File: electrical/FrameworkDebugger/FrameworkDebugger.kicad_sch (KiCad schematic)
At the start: 7 parts, among them J4 Conn_02x05_Odd_Even, J5 JST SH 1x4, U1 Teensy4.1

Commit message: updates to ee design
Signed-off-by: Kieran Levin <ktl@frame.work>
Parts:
- removed U1: Teensy4.1, teensy:Teensy41, symbol teensy:Teensy4.1
- added J1: USB_C_Receptacle, symbol Connector:USB_C_Receptacle
- added U2: RP2040, Package_DFN_QFN:QFN-56-1EP_7x7mm_P0.4mm_EP3.2x3.2mm, symbol MCU_RaspberryPi:RP2040
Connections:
- new net: J1.A1 (GND), J1.A12 (GND), J1.B1 (GND), J1.B12 (GND)
- new net: J1.A4 (VBUS), J1.A9 (VBUS), J1.B4 (VBUS), J1.B9 (VBUS)
- new net: U2.1 (IOVDD), U2.10 (IOVDD), U2.22 (IOVDD), U2.33 (IOVDD), U2.42 (IOVDD), U2.49 (IOVDD)
- new net: U2.23 (DVDD), U2.50 (DVDD)
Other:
- added sheet usb_c_passthrough (usb_c_passthrough.kicad_sch)

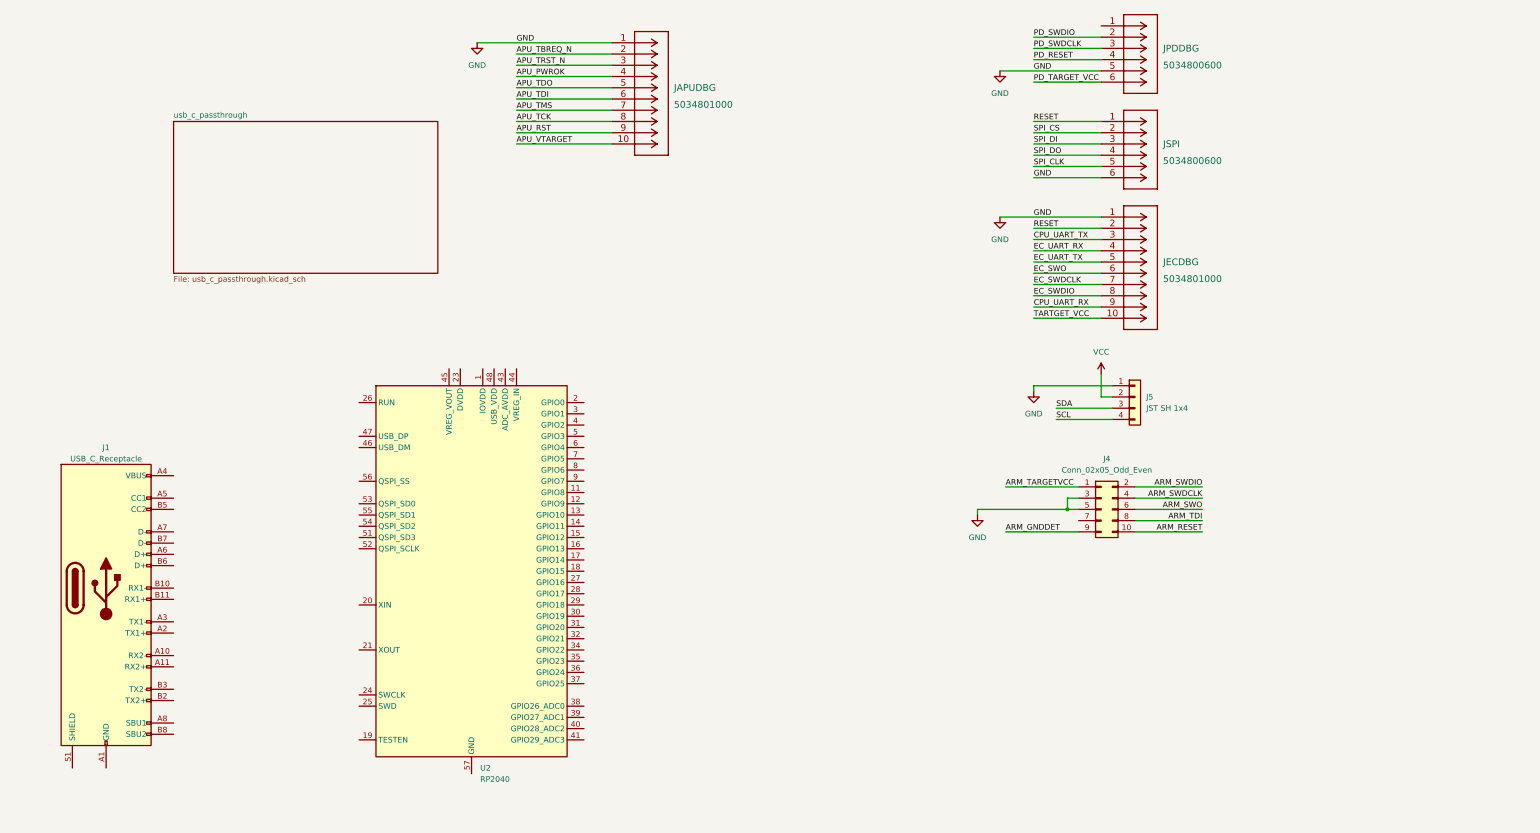
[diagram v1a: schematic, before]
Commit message: update design with rp2040
add type-c passthrough debug functionality
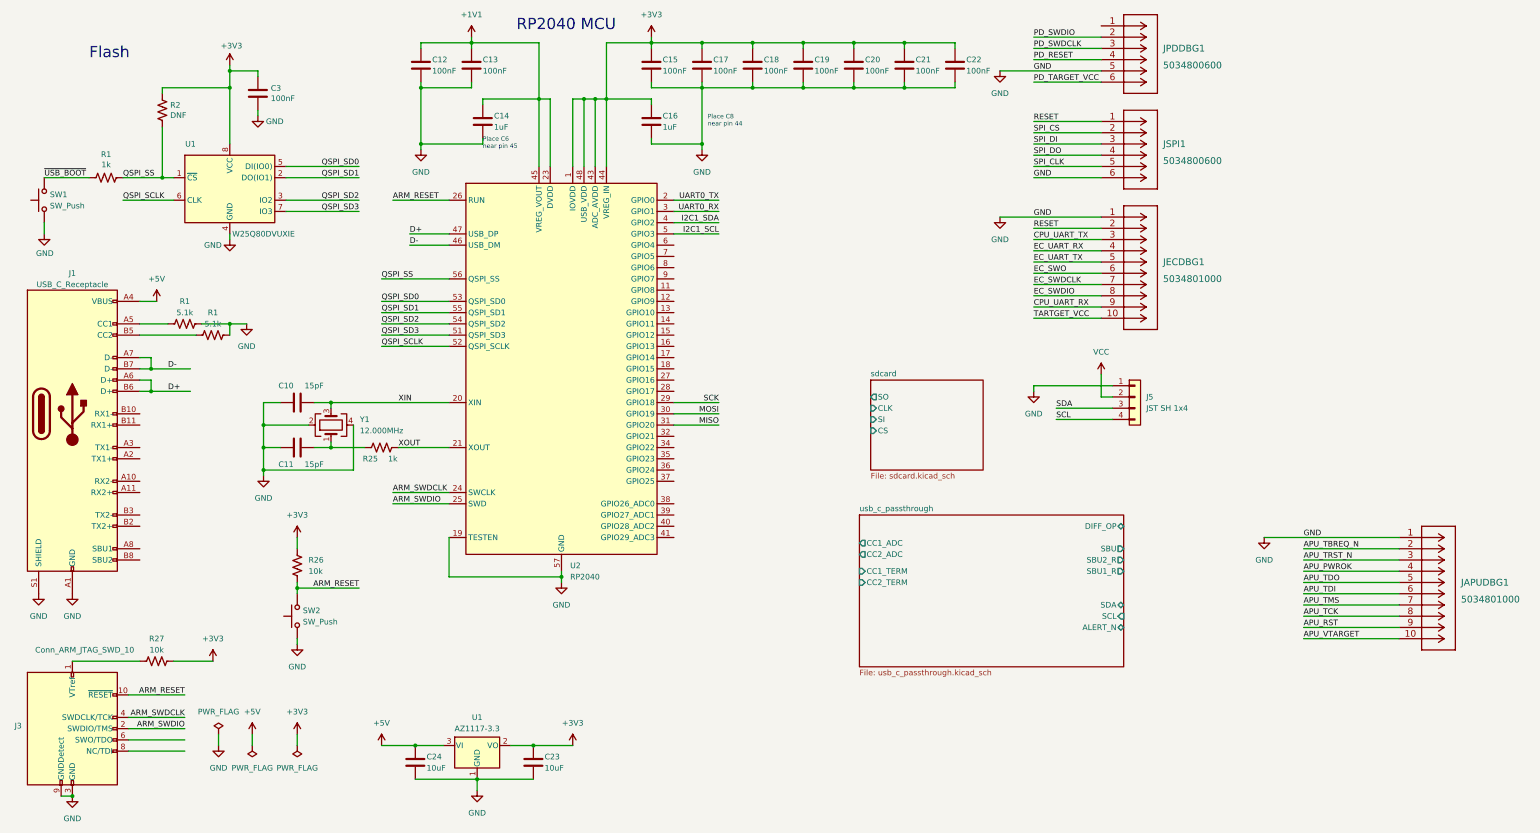
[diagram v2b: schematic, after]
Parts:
- removed J4: Conn_02x05_Odd_Even, symbol Connector_Generic:Conn_02x05_Odd_Even
- added C10, C11: 15pF, Capacitor_SMD:C_0402_1005Metric, symbol Device:C
- added C12, C13, C15, C17, C18, C19, C20, C21, C22, C3: 100nF, Capacitor_SMD:C_0402_1005Metric, symbol Device:C
- added C14, C16: 1uF, Capacitor_SMD:C_0402_1005Metric, symbol Device:C
- added C23, C24: 10uF, Capacitor_SMD:C_0603_1608Metric, symbol Device:C
- added J3: Conn_ARM_JTAG_SWD_10, symbol Connector:Conn_ARM_JTAG_SWD_10
- added R1: 1k, Capacitor_SMD:C_0402_1005Metric, symbol Device:R_US
- added R1 (x2): 5.1k, Resistor_SMD:R_0805_2012Metric, symbol Device:R_US
- added R2: DNF, Capacitor_SMD:C_0402_1005Metric, symbol Device:R_US
- added R25: 1k, Resistor_SMD:R_0402_1005Metric, symbol Device:R_US
- added R26, R27: 10k, Resistor_SMD:R_0402_1005Metric, symbol Device:R_US
- added SW1, SW2: SW_Push, Button_Switch_SMD:SW_SPST_CK_KXT3, symbol Switch:SW_Push
- added U1: W25Q80DVUXIE, Package_SO:SOIC-8_5.23x5.23mm_P1.27mm, symbol Memory_Flash:W25Q128JVS
- added U1: AZ1117-3.3, symbol Regulator_Linear:AZ1117-3.3
- added Y1: 12.000MHz, Crystal:Crystal_SMD_3225-4Pin_3.2x2.5mm, symbol Device:Crystal_GND24
- J1: footprint (none) -> Connector_USB:USB_C_Receptacle_GCT_USB4085
- renumbered JAPUDBG to JAPUDBG1, JECDBG to JECDBG1, JPDDBG to JPDDBG1, JSPI to JSPI1
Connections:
- net ARM_RESET: now also U2.26 (RUN), J3.10 (~{RESET}), R26.2, SW2.2
- net ARM_SWDCLK: now also U2.24 (SWCLK), J3.4 (SWDCLK/TCK)
- net ARM_SWDIO: now also U2.25 (SWD), J3.2 (SWDIO/TMS)
- net GND: now also J1.A1 (GND), J1.A12 (GND), J1.B1 (GND), J1.B12 (GND), J1.S1 (SHIELD), U2.19 (TESTEN), U2.57 (GND), C10.1, C11.1, C12.2, C13.2, C14.2, C15.2, C16.2, C17.2, C18.2, C19.2, C20.2, C21.2, C22.2, C23.2, C24.2, C3.2, J3.3 (GND), J3.5 (GND), J3.9 (GNDDetect), R1.2, R1.2, SW1.1, SW2.1, U1.1 (GND), U1.4 (GND), Y1.2, Y1.4
- net +5V: now reaches J1.A4 (VBUS), J1.A9 (VBUS), J1.B4 (VBUS), J1.B9 (VBUS)
- net +5V: now also C24.1, U1.3 (VI)
- net at J1.A5 (CC1): now also R1.1
- net D+: now reaches J1.A6 (D+)
- net D+: now also J1.B6 (D+), U2.47 (USB_DP)
- net D-: now reaches J1.A7 (D-)
- net D-: now also J1.B7 (D-), U2.46 (USB_DM)
- net at J1.B5 (CC2): now also R1.1
- net +3V3: now reaches U2.1 (IOVDD), U2.10 (IOVDD), U2.22 (IOVDD), U2.33 (IOVDD), U2.42 (IOVDD), U2.49 (IOVDD)
- net +3V3: now also U2.43 (ADC_AVDD), U2.44 (VREG_IN), U2.48 (USB_VDD), C15.1, C16.1, C17.1, C18.1, C19.1, C20.1, C21.1, C22.1, C23.1, C3.1, R2.1, R26.1, R27.2, U1.2 (VO), U1.8 (VCC)
- net UART0_TX: now reaches U2.2 (GPIO0)
- net XIN: now reaches U2.20 (XIN)
- net XIN: now also C10.2, Y1.3
- net XOUT: now reaches U2.21 (XOUT)
- net XOUT: now also R25.2
- net +1V1: now reaches U2.23 (DVDD), U2.50 (DVDD)
- net +1V1: now also U2.45 (VREG_VOUT), C12.1, C13.1, C14.1
- net SCK: now reaches U2.29 (GPIO18)
- net UART0_RX: now reaches U2.3 (GPIO1)
- net MOSI: now reaches U2.30 (GPIO19)
- net MISO: now reaches U2.31 (GPIO20)
- net I2C1_SDA: now reaches U2.4 (GPIO2)
- net I2C1_SCL: now reaches U2.5 (GPIO3)
- net QSPI_SD3: now reaches U2.51 (QSPI_SD3)
- net QSPI_SD3: now also U1.7 (IO3)
- net QSPI_SCLK: now reaches U2.52 (QSPI_SCLK)
- net QSPI_SCLK: now also U1.6 (CLK)
- net QSPI_SD0: now reaches U2.53 (QSPI_SD0)
- net QSPI_SD0: now also U1.5 (DI(IO0))
- net QSPI_SD2: now reaches U2.54 (QSPI_SD2)
- net QSPI_SD2: now also U1.3 (IO2)
- net QSPI_SD1: now reaches U2.55 (QSPI_SD1)
- net QSPI_SD1: now also U1.2 (DO(IO1))
- net QSPI_SS: now reaches U2.56 (QSPI_SS)
- net QSPI_SS: now also R1.1, R2.2, U1.1 (~{CS})
- new net: C11.2, R25.1, Y1.1
- new net: J3.1 (VTref), R27.1
- new net ~{USB_BOOT}: R1.2, SW1.2
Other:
- added sheet sdcard (sdcard.kicad_sch)
- sheet usb_c_passthrough ports: added ALERT_N, CC1_ADC, CC1_TERM, CC2_ADC, CC2_TERM, DIFF_OP, SBU, SBU1_R, SBU2_R, SCL, SDA; removed none
- note added: "Flash"
- note added: "Place C6 near pin 45"
- note added: "Place C8 near pin 44"
- note added: "RP2040 MCU"
- moved on the sheet: J1, JAPUDBG1, U2
